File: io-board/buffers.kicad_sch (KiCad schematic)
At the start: 16 parts

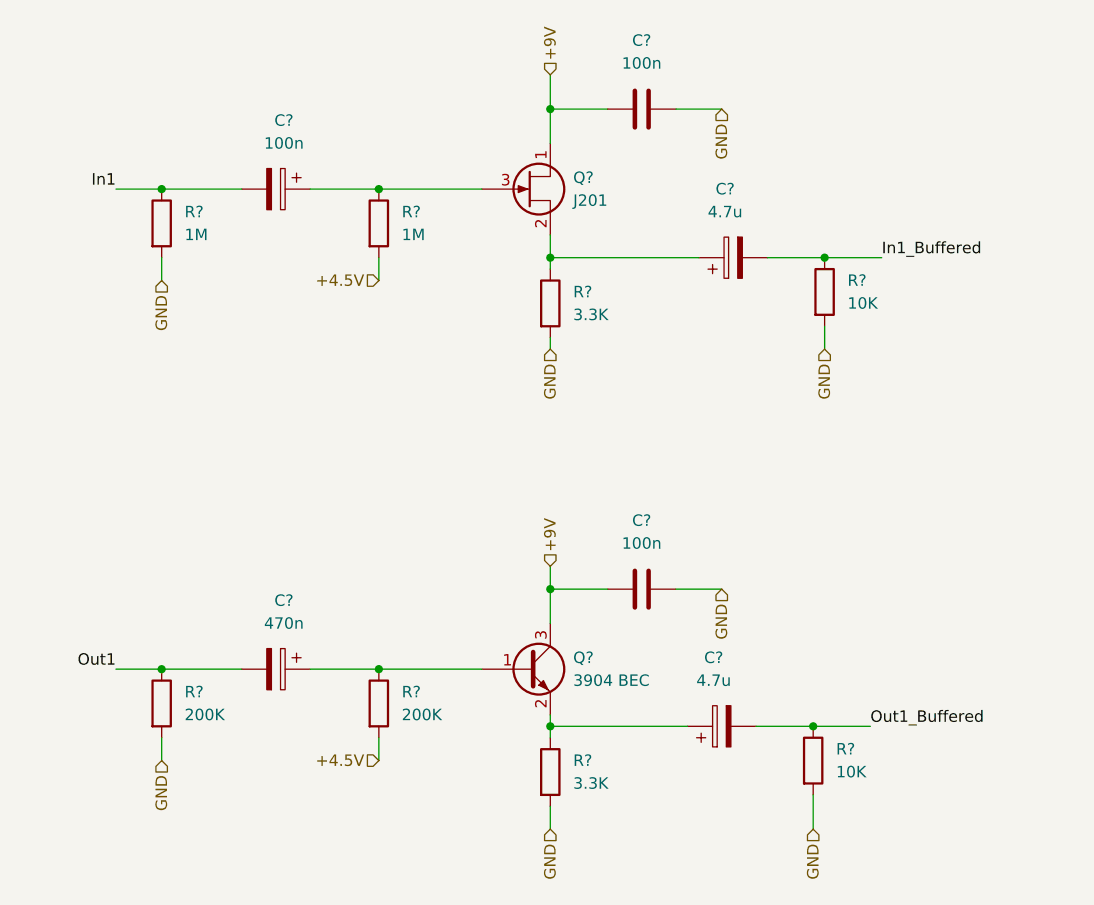
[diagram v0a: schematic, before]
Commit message: IO Board wip
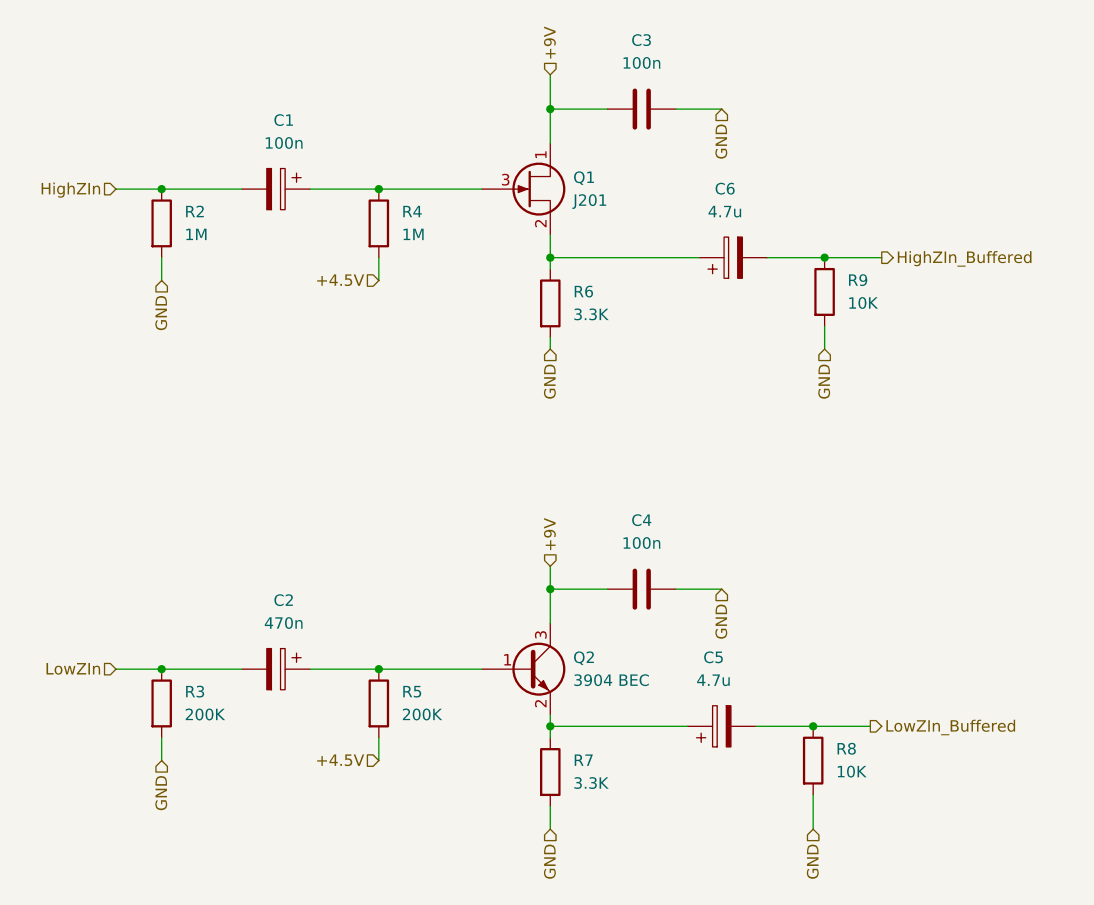
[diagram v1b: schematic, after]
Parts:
- C1, C2, C5, C6: renamed from C?; footprint (none) -> Capacitor_SMD:CP_Elec_4x5.4
- gave numbers to parts that had none: 12
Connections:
- net In1 renamed HighZIn
- net In1_Buffered renamed HighZIn_Buffered
- net Out1 renamed LowZIn
- net Out1_Buffered renamed LowZIn_Buffered
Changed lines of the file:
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@@
     (stroke (width 0) (type default) (color 0 0 0 0))
   )
-  (label "Out1_Buffered" (at 109.22 110.49 0)
-    (effects (font (size 1.27 1.27)) (justify left bottom))
-  )
-  (label "In1_Buffered" (at 110.49 58.42 0)
-    (effects (font (size 1.27 1.27)) (justify left bottom))
-  )
-  (label "In1" (at 25.4 50.8 180)
-    (effects (font (size 1.27 1.27)) (justify right bottom))
-  )
-  (label "Out1" (at 25.4 104.14 180)
-    (effects (font (size 1.27 1.27)) (justify right bottom))
+  (hierarchical_label "LowZIn_Buffered" (shape output) (at 109.22 110.49 0)
+    (effects (font (size 1.27 1.27)) (justify left))
   )
   (hierarchical_label "GND" (shape input) (at 92.71 41.91 270)
@@
     (effects (font (size 1.27 1.27)) (justify right))
   )
+  (hierarchical_label "HighZIn_Buffered" (shape output) (at 110.49 58.42 0)
+    (effects (font (size 1.27 1.27)) (justify left))
+  )
+  (hierarchical_label "HighZIn" (shape input) (at 25.4 50.8 180)
+    (effects (font (size 1.27 1.27)) (justify right))
+  )
   (hierarchical_label "+9V" (shape input) (at 73.66 38.1 90)
     (effects (font (size 1.27 1.27)) (justify left))
@@
     (effects (font (size 1.27 1.27)) (justify right))
   )
+  (hierarchical_label "LowZIn" (shape input) (at 25.4 104.14 180)
+    (effects (font (size 1.27 1.27)) (justify right))
+  )
   (hierarchical_label "GND" (shape input) (at 104.14 68.58 270)
     (effects (font (size 1.27 1.27)) (justify right))
@@
   (symbol (lib_id "Device:R") (at 102.87 114.3 0) (unit 1)
     (in_bom yes) (on_board yes) (fields_autoplaced)
-    (property "Reference" "R?" (id 0) (at 105.41 113.0299 0)
+    (property "Reference" "R8" (id 0) (at 105.41 113.0299 0)
       (effects (font (size 1.27 1.27)) (justify left))
     )
@@
   (symbol (lib_id "Device:Q_NPN_BEC") (at 71.12 104.14 0) (unit 1)
     (in_bom yes) (on_board yes) (fields_autoplaced)
-    (property "Reference" "Q?" (id 0) (at 76.2 102.8699 0)
+    (property "Reference" "Q2" (id 0) (at 76.2 102.8699 0)
       (effects (font (size 1.27 1.27)) (justify left))
     )
@@
   (symbol (lib_id "Device:R") (at 73.66 115.57 0) (unit 1)
     (in_bom yes) (on_board yes) (fields_autoplaced)
-    (property "Reference" "R?" (id 0) (at 76.2 114.2999 0)
+    (property "Reference" "R7" (id 0) (at 76.2 114.2999 0)
       (effects (font (size 1.27 1.27)) (justify left))
     )
@@
   (symbol (lib_id "Device:R") (at 54.61 107.95 0) (unit 1)
     (in_bom yes) (on_board yes) (fields_autoplaced)
-    (property "Reference" "R?" (id 0) (at 57.15 106.6799 0)
+    (property "Reference" "R5" (id 0) (at 57.15 106.6799 0)
       (effects (font (size 1.27 1.27)) (justify left))
     )
@@
   (symbol (lib_id "Device:R") (at 104.14 62.23 0) (unit 1)
     (in_bom yes) (on_board yes) (fields_autoplaced)
-    (property "Reference" "R?" (id 0) (at 106.68 60.9599 0)
+    (property "Reference" "R9" (id 0) (at 106.68 60.9599 0)
       (effects (font (size 1.27 1.27)) (justify left))
     )
@@
   (symbol (lib_id "Device:C_Polarized") (at 92.71 110.49 90) (unit 1)
     (in_bom yes) (on_board yes) (fields_autoplaced)
-    (property "Reference" "C?" (id 0) (at 91.821 102.87 90))
+    (property "Reference" "C5" (id 0) (at 91.821 102.87 90))
     (property "Value" "4.7u" (id 1) (at 91.821 105.41 90))
-    (property "Footprint" "" (id 2) (at 96.52 109.5248 0)
+    (property "Footprint" "Capacitor_SMD:CP_Elec_4x5.4" (id 2) (at 96.52 109.5248 0)
       (effects (font (size 1.27 1.27)) hide)
     )
@@
   (symbol (lib_id "Device:R") (at 30.48 107.95 0) (unit 1)
     (in_bom yes) (on_board yes) (fields_autoplaced)
-    (property "Reference" "R?" (id 0) (at 33.02 106.6799 0)
+    (property "Reference" "R3" (id 0) (at 33.02 106.6799 0)
       (effects (font (size 1.27 1.27)) (justify left))
     )
@@
   (symbol (lib_id "Device:C_Polarized") (at 43.18 50.8 270) (unit 1)
     (in_bom yes) (on_board yes) (fields_autoplaced)
-    (property "Reference" "C?" (id 0) (at 44.069 43.18 90))
+    (property "Reference" "C1" (id 0) (at 44.069 43.18 90))
     (property "Value" "100n" (id 1) (at 44.069 45.72 90))
-    (property "Footprint" "" (id 2) (at 39.37 51.7652 0)
+    (property "Footprint" "Capacitor_SMD:CP_Elec_4x5.4" (id 2) (at 39.37 51.7652 0)
       (effects (font (size 1.27 1.27)) hide)
     )
@@
   (symbol (lib_id "Device:C_Polarized") (at 93.98 58.42 90) (unit 1)
     (in_bom yes) (on_board yes) (fields_autoplaced)
-    (property "Reference" "C?" (id 0) (at 93.091 50.8 90))
+    (property "Reference" "C6" (id 0) (at 93.091 50.8 90))
     (property "Value" "4.7u" (id 1) (at 93.091 53.34 90))
-    (property "Footprint" "" (id 2) (at 97.79 57.4548 0)
+    (property "Footprint" "Capacitor_SMD:CP_Elec_4x5.4" (id 2) (at 97.79 57.4548 0)
       (effects (font (size 1.27 1.27)) hide)
     )
@@
   (symbol (lib_id "Device:Q_NJFET_DSG") (at 71.12 50.8 0) (unit 1)
     (in_bom yes) (on_board yes) (fields_autoplaced)
-    (property "Reference" "Q?" (id 0) (at 76.2 49.5299 0)
+    (property "Reference" "Q1" (id 0) (at 76.2 49.5299 0)
       (effects (font (size 1.27 1.27)) (justify left))
     )
@@
   (symbol (lib_id "Device:C") (at 83.82 41.91 90) (unit 1)
     (in_bom yes) (on_board yes) (fields_autoplaced)
-    (property "Reference" "C?" (id 0) (at 83.82 34.29 90))
+    (property "Reference" "C3" (id 0) (at 83.82 34.29 90))
     (property "Value" "100n" (id 1) (at 83.82 36.83 90))
     (property "Footprint" "Capacitor_SMD:C_0603_1608Metric_Pad1.08x0.95mm_HandSolder" (id 2) (at 87.63 40.9448 0)
@@
   (symbol (lib_id "Device:C_Polarized") (at 43.18 104.14 270) (unit 1)
     (in_bom yes) (on_board yes) (fields_autoplaced)
-    (property "Reference" "C?" (id 0) (at 44.069 96.52 90))
+    (property "Reference" "C2" (id 0) (at 44.069 96.52 90))
     (property "Value" "470n" (id 1) (at 44.069 99.06 90))
-    (property "Footprint" "" (id 2) (at 39.37 105.1052 0)
+    (property "Footprint" "Capacitor_SMD:CP_Elec_4x5.4" (id 2) (at 39.37 105.1052 0)
       (effects (font (size 1.27 1.27)) hide)
     )
@@
   (symbol (lib_id "Device:R") (at 54.61 54.61 0) (unit 1)
     (in_bom yes) (on_board yes) (fields_autoplaced)
-    (property "Reference" "R?" (id 0) (at 57.15 53.3399 0)
+    (property "Reference" "R4" (id 0) (at 57.15 53.3399 0)
       (effects (font (size 1.27 1.27)) (justify left))
     )
@@
   (symbol (lib_id "Device:R") (at 30.48 54.61 0) (unit 1)
     (in_bom yes) (on_board yes) (fields_autoplaced)
-    (property "Reference" "R?" (id 0) (at 33.02 53.3399 0)
+    (property "Reference" "R2" (id 0) (at 33.02 53.3399 0)
       (effects (font (size 1.27 1.27)) (justify left))
     )
@@
   (symbol (lib_id "Device:R") (at 73.66 63.5 0) (unit 1)
     (in_bom yes) (on_board yes) (fields_autoplaced)
-    (property "Reference" "R?" (id 0) (at 76.2 62.2299 0)
+    (property "Reference" "R6" (id 0) (at 76.2 62.2299 0)
       (effects (font (size 1.27 1.27)) (justify left))
     )
@@
   (symbol (lib_id "Device:C") (at 83.82 95.25 90) (unit 1)
     (in_bom yes) (on_board yes) (fields_autoplaced)
-    (property "Reference" "C?" (id 0) (at 83.82 87.63 90))
+    (property "Reference" "C4" (id 0) (at 83.82 87.63 90))
     (property "Value" "100n" (id 1) (at 83.82 90.17 90))
     (property "Footprint" "Capacitor_SMD:C_0603_1608Metric_Pad1.08x0.95mm_HandSolder" (id 2) (at 87.63 94.2848 0)

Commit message: Fixed buffers
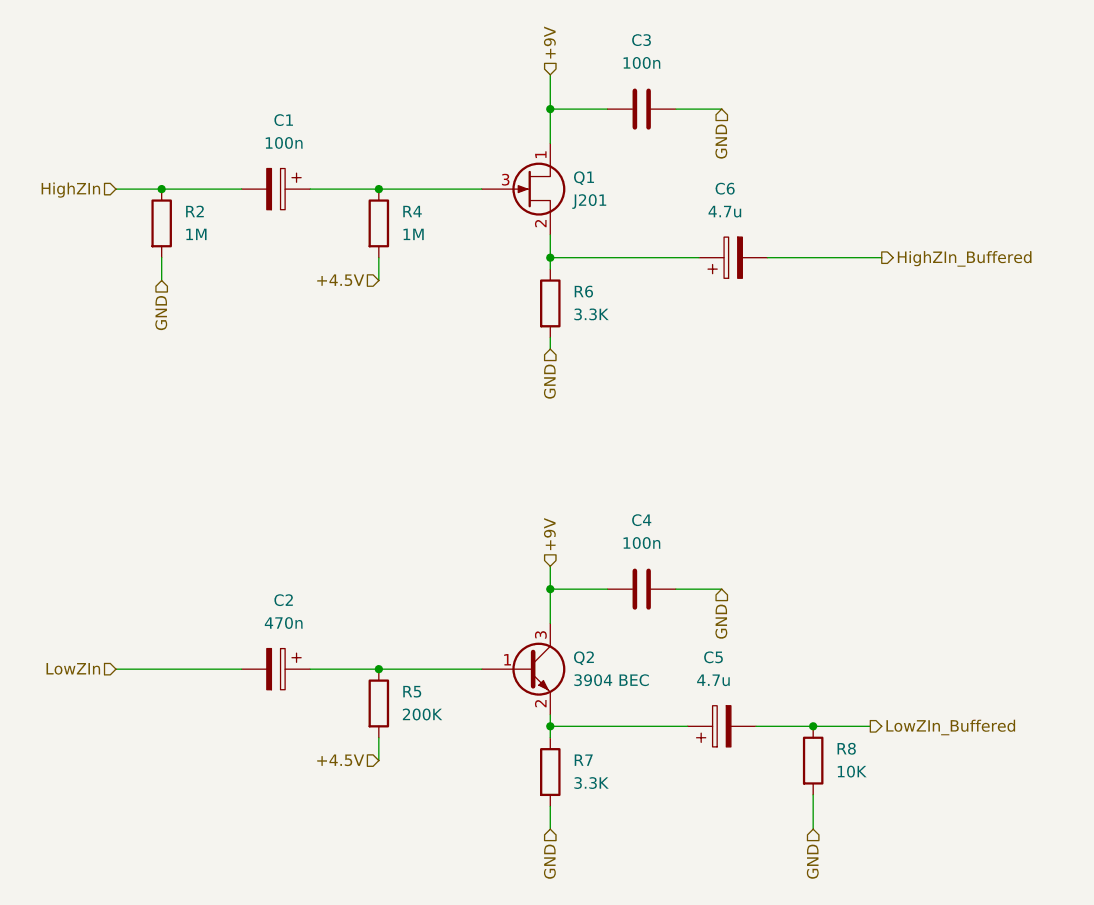
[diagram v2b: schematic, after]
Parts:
- removed R3: 200K, Resistor_SMD:R_0603_1608Metric_Pad0.98x0.95mm_HandSolder, symbol Device:R
- removed R9: 10K, Resistor_SMD:R_0603_1608Metric_Pad0.98x0.95mm_HandSolder, symbol Device:R
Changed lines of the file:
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@@
 (kicad_sch (version 20211123) (generator eeschema)
   (paper "A4")
-  (junction (at 30.48 104.14) (diameter 0) (color 0 0 0 0)
-  )
   (junction (at 102.87 110.49) (diameter 0) (color 0 0 0 0)
   )
@@
   (junction (at 73.66 41.91) (diameter 0) (color 0 0 0 0)
   )
-  (junction (at 104.14 58.42) (diameter 0) (color 0 0 0 0)
-  )
   (junction (at 73.66 95.25) (diameter 0) (color 0 0 0 0)
   )
@@
   (junction (at 73.66 110.49) (diameter 0) (color 0 0 0 0)
   )
-  (wire (pts (xy 30.48 111.76) (xy 30.48 114.3))
-    (stroke (width 0) (type default) (color 0 0 0 0))
-  )
-  (wire (pts (xy 104.14 58.42) (xy 110.49 58.42))
+  (wire (pts (xy 97.79 58.42) (xy 110.49 58.42))
     (stroke (width 0) (type default) (color 0 0 0 0))
   )
@@
     (stroke (width 0) (type default) (color 0 0 0 0))
   )
-  (wire (pts (xy 25.4 104.14) (xy 30.48 104.14))
-    (stroke (width 0) (type default) (color 0 0 0 0))
-  )
-  (wire (pts (xy 30.48 104.14) (xy 39.37 104.14))
+  (wire (pts (xy 25.4 104.14) (xy 39.37 104.14))
     (stroke (width 0) (type default) (color 0 0 0 0))
   )
@@
     (stroke (width 0) (type default) (color 0 0 0 0))
   )
-  (wire (pts (xy 97.79 58.42) (xy 104.14 58.42))
-    (stroke (width 0) (type default) (color 0 0 0 0))
-  )
   (wire (pts (xy 73.66 95.25) (xy 73.66 99.06))
     (stroke (width 0) (type default) (color 0 0 0 0))
@@
     (stroke (width 0) (type default) (color 0 0 0 0))
   )
-  (wire (pts (xy 104.14 66.04) (xy 104.14 68.58))
-    (stroke (width 0) (type default) (color 0 0 0 0))
-  )
   (wire (pts (xy 54.61 111.76) (xy 54.61 114.3))
     (stroke (width 0) (type default) (color 0 0 0 0))
@@
     (effects (font (size 1.27 1.27)) (justify left))
   )
-  (hierarchical_label "GND" (shape input) (at 30.48 114.3 270)
-    (effects (font (size 1.27 1.27)) (justify right))
-  )
   (hierarchical_label "GND" (shape input) (at 73.66 68.58 270)
     (effects (font (size 1.27 1.27)) (justify right))
@@
     (effects (font (size 1.27 1.27)) (justify right))
   )
-  (hierarchical_label "GND" (shape input) (at 104.14 68.58 270)
-    (effects (font (size 1.27 1.27)) (justify right))
-  )
   (hierarchical_label "+4.5V" (shape input) (at 54.61 60.96 180)
     (effects (font (size 1.27 1.27)) (justify right))
@@
     )
     (property "LCSC" "C203392" (id 4) (at 54.61 107.95 0)
-      (effects (font (size 1.27 1.27)) hide)
-    )
-    (pin "1")
-    (pin "2")
-  )
-  (symbol (lib_id "Device:R") (at 104.14 62.23 0) (unit 1)
-    (in_bom yes) (on_board yes) (fields_autoplaced)
-    (property "Reference" "R9" (id 0) (at 106.68 60.9599 0)
-      (effects (font (size 1.27 1.27)) (justify left))
-    )
-    (property "Value" "10K" (id 1) (at 106.68 63.4999 0)
-      (effects (font (size 1.27 1.27)) (justify left))
-    )
-    (property "Footprint" "Resistor_SMD:R_0603_1608Metric_Pad0.98x0.95mm_HandSolder" (id 2) (at 102.362 62.23 90)
-      (effects (font (size 1.27 1.27)) hide)
-    )
-    (property "Datasheet" "~" (id 3) (at 104.14 62.23 0)
-      (effects (font (size 1.27 1.27)) hide)
-    )
-    (property "LCSC" "C203392" (id 4) (at 104.14 62.23 0)
       (effects (font (size 1.27 1.27)) hide)
     )
@@
       (effects (font (size 1.27 1.27)) hide)
     )
-    (pin "1")
-    (pin "2")
-  )
-  (symbol (lib_id "Device:R") (at 30.48 107.95 0) (unit 1)
-    (in_bom yes) (on_board yes) (fields_autoplaced)
-    (property "Reference" "R3" (id 0) (at 33.02 106.6799 0)
-      (effects (font (size 1.27 1.27)) (justify left))
-    )
-    (property "Value" "200K" (id 1) (at 33.02 109.2199 0)
-      (effects (font (size 1.27 1.27)) (justify left))
-    )
-    (property "Footprint" "Resistor_SMD:R_0603_1608Metric_Pad0.98x0.95mm_HandSolder" (id 2) (at 28.702 107.95 90)
-      (effects (font (size 1.27 1.27)) hide)
-    )
-    (property "Datasheet" "~" (id 3) (at 30.48 107.95 0)
-      (effects (font (size 1.27 1.27)) hide)
-    )
-    (property "LCSC" "C234360" (id 4) (at 30.48 107.95 0)
-      (effects (font (size 1.27 1.27)) hide)
-    )

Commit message: wip
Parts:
- C5, C6: Mouser (none) -> 710-865080540002
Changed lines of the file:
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@@
+      (effects (font (size 1.27 1.27)) hide)
+    )
+    (property "Mouser" "710-865080540002" (id 4) (at 92.71 110.49 0)
       (effects (font (size 1.27 1.27)) hide)
     )
@@
       (effects (font (size 1.27 1.27)) hide)
     )
+    (property "Mouser" "710-865080540002" (id 4) (at 93.98 58.42 0)
+      (effects (font (size 1.27 1.27)) hide)
+    )

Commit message: io jlc part numbers
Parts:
- C2: LCSC (none) -> C305350
- C5, C6: LCSC (none) -> C2963050
- R2, R4: LCSC C234360 -> C105578
- R5: LCSC C203392 -> C25811
- R6, R7: LCSC C144661 -> C22978
- R8: LCSC C203392 -> C25804
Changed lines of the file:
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@@
       (effects (font (size 1.27 1.27)) hide)
     )
-    (property "LCSC" "C203392" (id 4) (at 102.87 114.3 0)
+    (property "LCSC" "C25804" (id 4) (at 102.87 114.3 0)
       (effects (font (size 1.27 1.27)) hide)
     )
@@
       (effects (font (size 1.27 1.27)) hide)
     )
-    (property "LCSC" "C144661" (id 4) (at 73.66 115.57 0)
+    (property "LCSC" "C22978" (id 4) (at 73.66 115.57 0)
       (effects (font (size 1.27 1.27)) hide)
     )
@@
       (effects (font (size 1.27 1.27)) hide)
     )
-    (property "LCSC" "C203392" (id 4) (at 54.61 107.95 0)
+    (property "LCSC" "C25811" (id 4) (at 54.61 107.95 0)
       (effects (font (size 1.27 1.27)) hide)
     )
@@
       (effects (font (size 1.27 1.27)) hide)
     )
+    (property "LCSC" "C2963050" (id 5) (at 92.71 110.49 0)
+      (effects (font (size 1.27 1.27)) hide)
+    )
     (pin "1")
     (pin "2")
@@
       (effects (font (size 1.27 1.27)) hide)
     )
+    (property "LCSC" "C2963050" (id 5) (at 93.98 58.42 0)
+      (effects (font (size 1.27 1.27)) hide)
+    )
     (pin "1")
     (pin "2")
@@
       (effects (font (size 1.27 1.27)) hide)
     )
+    (property "LCSC" "C305350" (id 4) (at 43.18 104.14 0)
+      (effects (font (size 1.27 1.27)) hide)
+    )
     (pin "1")
     (pin "2")
@@
       (effects (font (size 1.27 1.27)) hide)
     )
-    (property "LCSC" "C234360" (id 4) (at 54.61 54.61 0)
+    (property "LCSC" "C105578" (id 4) (at 54.61 54.61 0)
       (effects (font (size 1.27 1.27)) hide)
     )
@@
       (effects (font (size 1.27 1.27)) hide)
     )
-    (property "LCSC" "C234360" (id 4) (at 30.48 54.61 0)
+    (property "LCSC" "C105578" (id 4) (at 30.48 54.61 0)
       (effects (font (size 1.27 1.27)) hide)
     )
@@
       (effects (font (size 1.27 1.27)) hide)
     )
-    (property "LCSC" "C144661" (id 4) (at 73.66 63.5 0)
-      (effects (font (size 1.27 1.27)) hide)
-    )
+    (property "LCSC" "C22978" (id 4) (at 73.66 63.5 0)
+      (effects (font (size 1.27 1.27)) hide)
+    )

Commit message: JLC got 100n caps
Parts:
- C1: LCSC (none) -> C271438
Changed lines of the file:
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@@
+      (effects (font (size 1.27 1.27)) hide)
+    )
+    (property "LCSC" "C271438" (id 4) (at 43.18 50.8 0)
       (effects (font (size 1.27 1.27)) hide)
     )

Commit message: Protato updates and schem
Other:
- company: (none) -> Andrei Salomatin / Pedal Markt
- title: (none) -> Protato
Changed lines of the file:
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@@
 (kicad_sch (version 20211123) (generator eeschema)
   (paper "A4")
+  (title_block
+    (title "Protato")
+    (rev "v1rev1")
+    (company "Andrei Salomatin / Pedal Markt")
+  )
   (junction (at 102.87 110.49) (diameter 0) (color 0 0 0 0)
   )
